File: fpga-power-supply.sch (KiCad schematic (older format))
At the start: 86 parts, among them U14 XC7A100T-FGG484

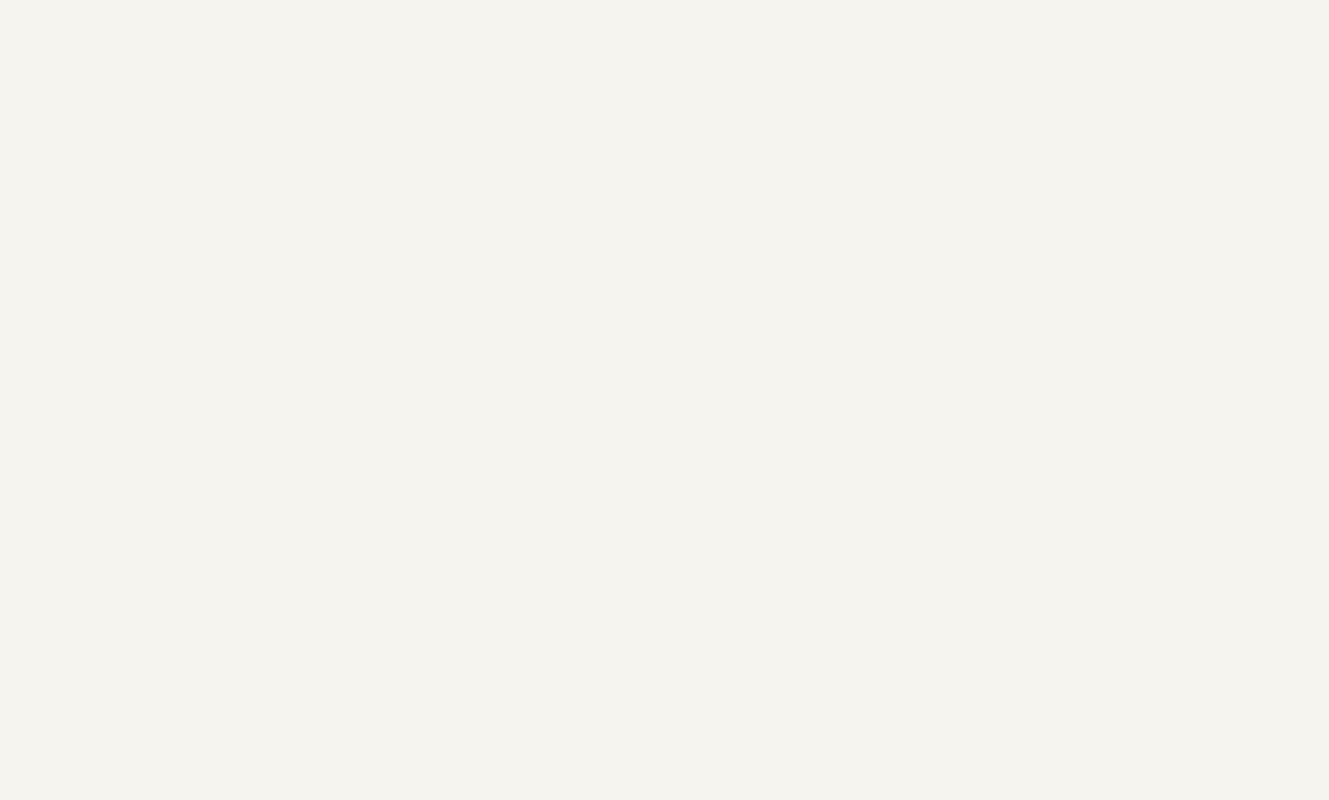
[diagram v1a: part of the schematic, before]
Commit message: Fixed PCIe x1 connection
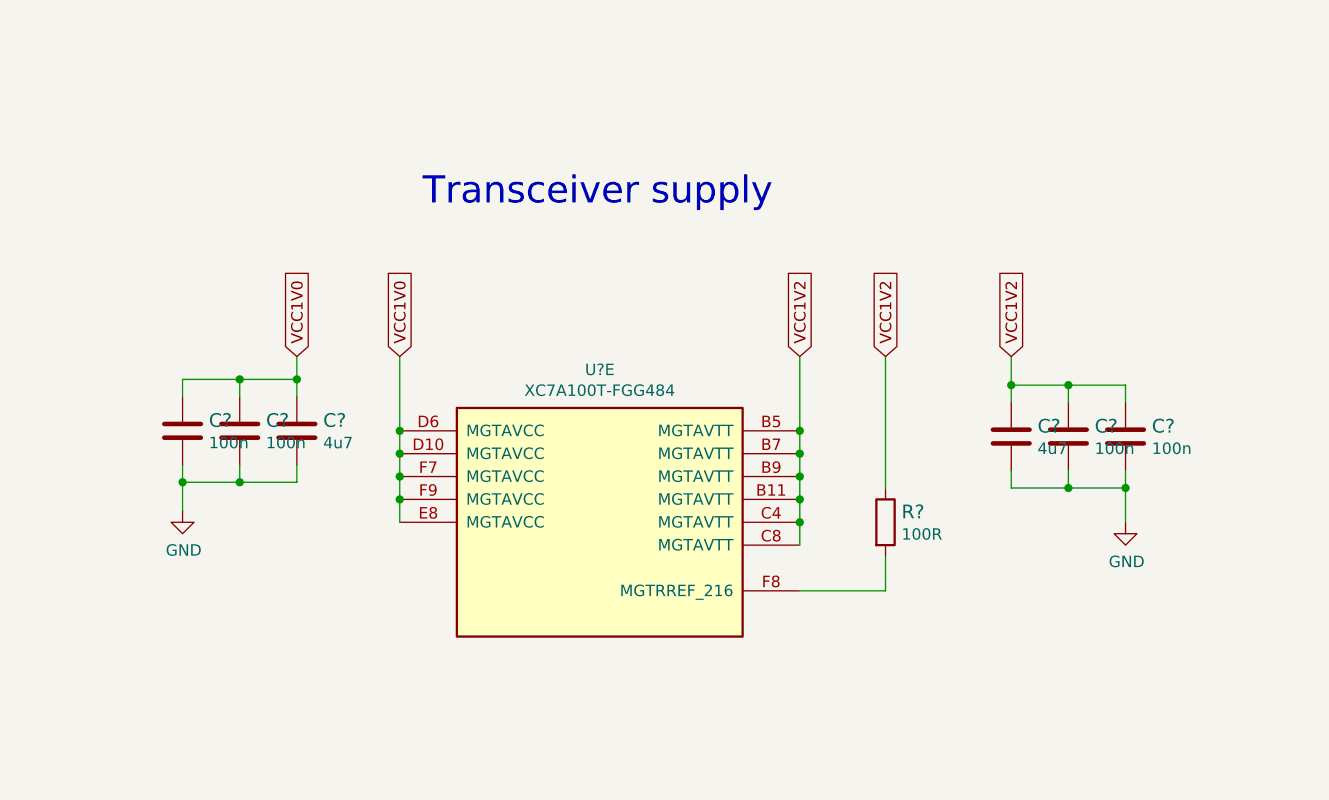
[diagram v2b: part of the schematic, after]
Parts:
- added C? (x2): C_4u7_0603, artix-dc-scm-footprints:0603-cap, symbol artix-dc-scm:C_4u7_0603
- added C? (x4): C_100n_0402, antmicro-footprints:0402-cap, symbol artix-dc-scm:C_100n_0402
- added R?: R_100R_0402, artix-dc-scm-footprints:0402-res, symbol artix-dc-scm:R_100R_0402
- added U?: XC7A100T-FGG484, artix-dc-scm-footprints:Xilinx_FGG484, symbol artix-dc-scm:XC7A100T-FGG484
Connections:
- net GND: now also C?.2, C?.2, C?.2, C?.2, C?.2, C?.2
- new net: R?.2, U?.F8 (MGTRREF_216)
- new net VCC1V0: C?.1, C?.1, C?.1, U?.D10 (MGTAVCC), U?.D6 (MGTAVCC), U?.E8 (MGTAVCC), U?.F7 (MGTAVCC), U?.F9 (MGTAVCC)
- new net VCC1V2: C?.1, C?.1, C?.1, R?.1, U?.B11 (MGTAVTT), U?.B5 (MGTAVTT), U?.B7 (MGTAVTT), U?.B9 (MGTAVTT), U?.C4 (MGTAVTT), U?.C8 (MGTAVTT)
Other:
- note added: "Transceiver supply"

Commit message: Added local libs
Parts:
- gave numbers to parts that had none: 8
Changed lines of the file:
@@
 P 12200 7800
 AR Path="/614223A1/6036C315" Ref="U?"  Part="5"
-AR Path="/5FD86C51/6036C315" Ref="U?"  Part="5"
-F 0 "U?" H 12625 8467 50  0000 C CNN
+AR Path="/5FD86C51/6036C315" Ref="U14"  Part="5"
+F 0 "U14" H 12625 8467 50  0000 C CNN
 F 1 "XC7A100T-FGG484" H 12625 8376 50  0000 C CNN
 F 2 "artix-dc-scm-footprints:Xilinx_FGG484" H 11900 7800 50  0001 C CNN
@@
 $EndComp
 $Comp
-L artix-dc-scm:R_100R_0402 R?
+L artix-dc-scm:R_100R_0402 R143
 U 1 1 605D9E2A
 P 13875 7800
-F 0 "R?" V 13830 7870 60  0000 L CNN
+F 0 "R143" V 13830 7870 60  0000 L CNN
 F 1 "R_100R_0402" H 13875 7650 60  0001 C CNN
 F 2 "artix-dc-scm-footprints:0402-res" H 14075 8000 60  0001 L CNN
@@
 AR Path="/605FD480/607C52B1" Ref="C?"  Part="1"
 AR Path="/60633613/607C52B1" Ref="C?"  Part="1"
-AR Path="/5FD86C51/607C52B1" Ref="C?"  Part="1"
-F 0 "C?" H 14540 7470 60  0000 L CNN
+AR Path="/5FD86C51/607C52B1" Ref="C191"  Part="1"
+F 0 "C191" H 14540 7470 60  0000 L CNN
 F 1 "C_4u7_0603" H 14425 7275 60  0001 C CNN
 F 2 "artix-dc-scm-footprints:0603-cap" H 14625 7625 60  0001 L CNN
@@
 $EndComp
 $Comp
-L artix-dc-scm:C_100n_0402 C?
+L artix-dc-scm:C_100n_0402 C192
 U 1 1 607F3D6A
 P 14675 7425
-F 0 "C?" H 14790 7470 60  0000 L CNN
+F 0 "C192" H 14790 7470 60  0000 L CNN
 F 1 "C_100n_0402" H 14675 7275 60  0001 C CNN
 F 2 "antmicro-footprints:0402-cap" H 14875 7625 60  0001 L CNN
@@
 $EndComp
 $Comp
-L artix-dc-scm:C_100n_0402 C?
+L artix-dc-scm:C_100n_0402 C193
 U 1 1 607F45D3
 P 14925 7425
-F 0 "C?" H 15040 7470 60  0000 L CNN
+F 0 "C193" H 15040 7470 60  0000 L CNN
 F 1 "C_100n_0402" H 14925 7275 60  0001 C CNN
 F 2 "antmicro-footprints:0402-cap" H 15125 7625 60  0001 L CNN
@@
 AR Path="/605FD480/60834105" Ref="C?"  Part="1"
 AR Path="/60633613/60834105" Ref="C?"  Part="1"
-AR Path="/5FD86C51/60834105" Ref="C?"  Part="1"
-F 0 "C?" H 11415 7445 60  0000 L CNN
+AR Path="/5FD86C51/60834105" Ref="C190"  Part="1"
+F 0 "C190" H 11415 7445 60  0000 L CNN
 F 1 "C_4u7_0603" H 11300 7250 60  0001 C CNN
 F 2 "artix-dc-scm-footprints:0603-cap" H 11500 7600 60  0001 L CNN
@@
 $EndComp
 $Comp
-L artix-dc-scm:C_100n_0402 C?
+L artix-dc-scm:C_100n_0402 C136
 U 1 1 6083962C
 P 11050 7400
-F 0 "C?" H 11165 7445 60  0000 L CNN
+F 0 "C136" H 11165 7445 60  0000 L CNN
 F 1 "C_100n_0402" H 11050 7250 60  0001 C CNN
 F 2 "antmicro-footprints:0402-cap" H 11250 7600 60  0001 L CNN
@@
 $EndComp
 $Comp
-L artix-dc-scm:C_100n_0402 C?
+L artix-dc-scm:C_100n_0402 C134
 U 1 1 6083EFEF
 P 10800 7400
-F 0 "C?" H 10915 7445 60  0000 L CNN
+F 0 "C134" H 10915 7445 60  0000 L CNN
 F 1 "C_100n_0402" H 10800 7250 60  0001 C CNN
 F 2 "antmicro-footprints:0402-cap" H 11000 7600 60  0001 L CNN
@@
 AR Path="/605FD480/60B225B3" Ref="#PWR?"  Part="1"
 AR Path="/60633613/60B225B3" Ref="#PWR?"  Part="1"
-AR Path="/5FD86C51/60B225B3" Ref="#PWR?"  Part="1"
-F 0 "#PWR?" H 10800 7500 50  0001 C CNN
+AR Path="/5FD86C51/60B225B3" Ref="#PWR0120"  Part="1"
+F 0 "#PWR0120" H 10800 7500 50  0001 C CNN
 F 1 "GND" H 10805 7577 50  0000 C CNN
 F 2 "" H 10800 7750 50  0001 C CNN
@@
 AR Path="/605FD480/60BAB37F" Ref="#PWR?"  Part="1"
 AR Path="/60633613/60BAB37F" Ref="#PWR?"  Part="1"
-AR Path="/5FD86C51/60BAB37F" Ref="#PWR?"  Part="1"
-F 0 "#PWR?" H 14925 7550 50  0001 C CNN
+AR Path="/5FD86C51/60BAB37F" Ref="#PWR0121"  Part="1"
+F 0 "#PWR0121" H 14925 7550 50  0001 C CNN
 F 1 "GND" H 14930 7627 50  0000 C CNN
 F 2 "" H 14925 7800 50  0001 C CNN

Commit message: Update component libraries
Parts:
- C134, C136, C192, C193: footprint antmicro-footprints:0402-cap -> artix-dc-scm-footprints:0402-cap; symbol artix-dc-scm:C_100n_0402 -> artix-dc-scm:C_100n_0402-artix-dc-scm
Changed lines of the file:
@@
 Connection ~ 3250 3350
 $Comp
-L artix-dc-scm:GND #PWR?
+L artix-dc-scm:GND-artix-dc-scm #PWR?
 U 1 1 6166233A
 P 3250 3500
@@
 Connection ~ 3250 4500
 $Comp
-L artix-dc-scm:GND #PWR?
+L artix-dc-scm:GND-artix-dc-scm #PWR?
 U 1 1 61665D3D
 P 3250 4650
@@
 Connection ~ 3250 5600
 $Comp
-L artix-dc-scm:GND #PWR?
+L artix-dc-scm:GND-artix-dc-scm #PWR?
 U 1 1 6166A10D
 P 3250 5750
@@
 Connection ~ 3250 6700
 $Comp
-L artix-dc-scm:GND #PWR?
+L artix-dc-scm:GND-artix-dc-scm #PWR?
 U 1 1 6166E6C7
 P 3250 6850
@@
 Connection ~ 3250 7800
 $Comp
-L artix-dc-scm:GND #PWR?
+L artix-dc-scm:GND-artix-dc-scm #PWR?
 U 1 1 61674524
 P 3250 7950
@@
 	7750 8700 7750 9000
 $Comp
-L artix-dc-scm:GND #PWR?
+L artix-dc-scm:GND-artix-dc-scm #PWR?
 U 1 1 6167CA21
 P 3250 9050
@@
 $EndComp
 $Comp
-L artix-dc-scm:GND #PWR?
+L artix-dc-scm:GND-artix-dc-scm #PWR?
 U 1 1 6175DADD
 P 7750 9000
@@
 	9750 8700 9750 9000
 $Comp
-L artix-dc-scm:GND #PWR?
+L artix-dc-scm:GND-artix-dc-scm #PWR?
 U 1 1 61771DD8
 P 9750 9000
@@
 	6750 3250 7050 3250
 $Comp
-L artix-dc-scm:GND #PWR?
+L artix-dc-scm:GND-artix-dc-scm #PWR?
 U 1 1 61BBB7F0
 P 7050 3400
@@
 	15050 5000 15350 5000
 $Comp
-L artix-dc-scm:GND #PWR?
+L artix-dc-scm:GND-artix-dc-scm #PWR?
 U 1 1 627B33DD
 P 15350 5200
@@
 	15050 3700 15350 3700
 $Comp
-L artix-dc-scm:GND #PWR?
+L artix-dc-scm:GND-artix-dc-scm #PWR?
 U 1 1 62810E19
 P 15350 3850
@@
 200T
 $Comp
-L artix-dc-scm:GND #PWR?
+L artix-dc-scm:GND-artix-dc-scm #PWR?
 U 1 1 62E6DC2F
 P 11000 3550
@@
 $EndComp
 $Comp
-L artix-dc-scm:GND #PWR?
+L artix-dc-scm:GND-artix-dc-scm #PWR?
 U 1 1 6077E24E
 P 6900 5200
@@
 $EndComp
 $Comp
-L artix-dc-scm:GND #PWR?
+L artix-dc-scm:GND-artix-dc-scm #PWR?
 U 1 1 61075D45
 P 7350 3500
@@
 $EndComp
 $Comp
-L artix-dc-scm:C_100n_0402 C192
+L artix-dc-scm:C_100n_0402-artix-dc-scm C192
 U 1 1 607F3D6A
 P 14675 7425
 F 0 "C192" H 14790 7470 60  0000 L CNN
 F 1 "C_100n_0402" H 14675 7275 60  0001 C CNN
-F 2 "antmicro-footprints:0402-cap" H 14875 7625 60  0001 L CNN
+F 2 "artix-dc-scm-footprints:0402-cap" H 14875 7625 60  0001 L CNN
 F 3 "" H 14675 7425 50  0001 C CNN
 F 4 "Walsin" H 14875 7825 60  0001 L CNN "Manufacturer"
@@
 $EndComp
 $Comp
-L artix-dc-scm:C_100n_0402 C193
+L artix-dc-scm:C_100n_0402-artix-dc-scm C193
 U 1 1 607F45D3
 P 14925 7425
 F 0 "C193" H 15040 7470 60  0000 L CNN
 F 1 "C_100n_0402" H 14925 7275 60  0001 C CNN
-F 2 "antmicro-footprints:0402-cap" H 15125 7625 60  0001 L CNN
+F 2 "artix-dc-scm-footprints:0402-cap" H 15125 7625 60  0001 L CNN
 F 3 "" H 14925 7425 50  0001 C CNN
 F 4 "Walsin" H 15125 7825 60  0001 L CNN "Manufacturer"
@@
 $EndComp
 $Comp
-L artix-dc-scm:C_100n_0402 C136
+L artix-dc-scm:C_100n_0402-artix-dc-scm C136
 U 1 1 6083962C
 P 11050 7400
 F 0 "C136" H 11165 7445 60  0000 L CNN
 F 1 "C_100n_0402" H 11050 7250 60  0001 C CNN
-F 2 "antmicro-footprints:0402-cap" H 11250 7600 60  0001 L CNN
+F 2 "artix-dc-scm-footprints:0402-cap" H 11250 7600 60  0001 L CNN
 F 3 "" H 11050 7400 50  0001 C CNN
 F 4 "Walsin" H 11250 7800 60  0001 L CNN "Manufacturer"
@@
 $EndComp
 $Comp
-L artix-dc-scm:C_100n_0402 C134
+L artix-dc-scm:C_100n_0402-artix-dc-scm C134
 U 1 1 6083EFEF
 P 10800 7400
 F 0 "C134" H 10915 7445 60  0000 L CNN
 F 1 "C_100n_0402" H 10800 7250 60  0001 C CNN
-F 2 "antmicro-footprints:0402-cap" H 11000 7600 60  0001 L CNN
+F 2 "artix-dc-scm-footprints:0402-cap" H 11000 7600 60  0001 L CNN
 F 3 "" H 10800 7400 50  0001 C CNN
 F 4 "Walsin" H 11000 7800 60  0001 L CNN "Manufacturer"
@@
 Connection ~ 10800 7625
 $Comp
-L artix-dc-scm:GND #PWR?
+L artix-dc-scm:GND-artix-dc-scm #PWR?
 U 1 1 60B225B3
 P 10800 7750
@@
 $EndComp
 $Comp
-L artix-dc-scm:GND #PWR?
+L artix-dc-scm:GND-artix-dc-scm #PWR?
 U 1 1 60BAB37F
 P 14925 7800
